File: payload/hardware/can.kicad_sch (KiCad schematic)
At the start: 2 parts, among them U2 MCP2517FD-xJHA, U4 SN65HVD230

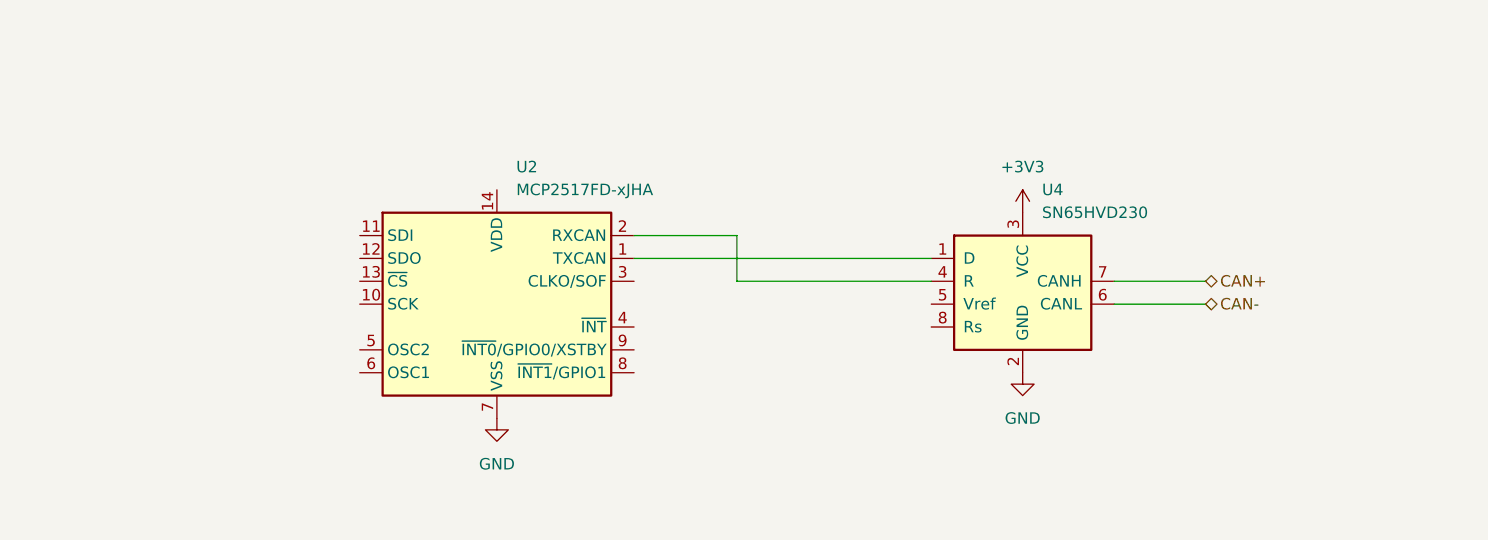
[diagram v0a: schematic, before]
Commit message: add part of a motor driver
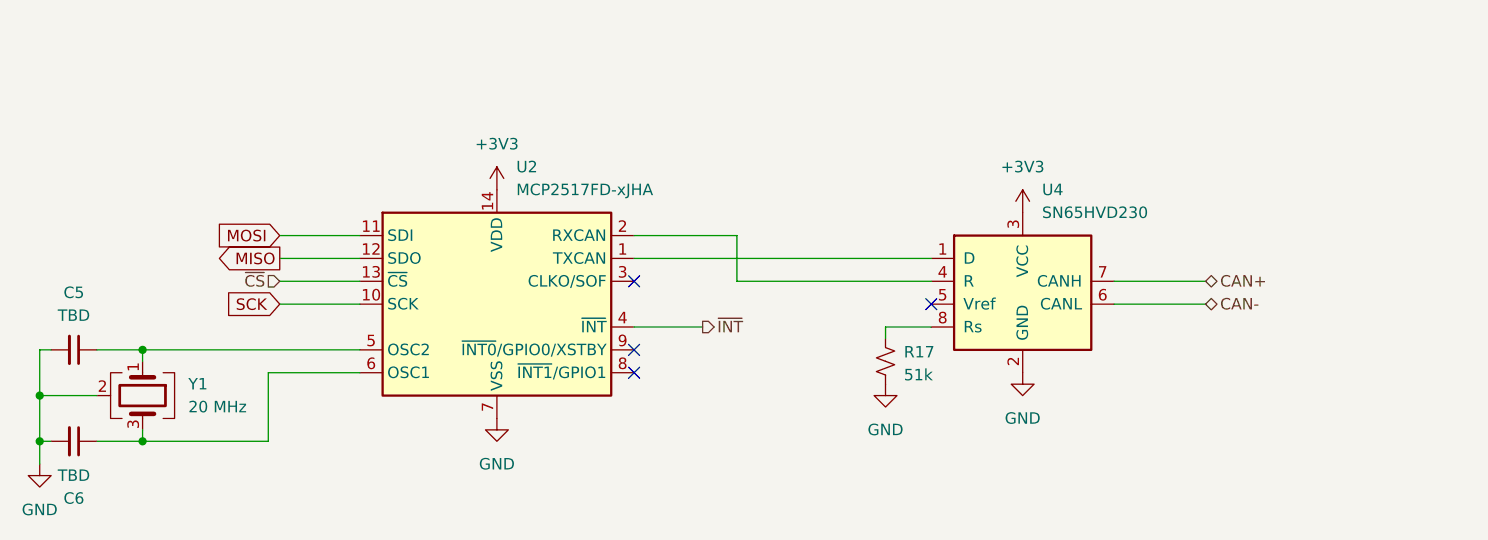
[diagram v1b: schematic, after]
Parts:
- added C5, C6: TBD, Capacitor_SMD:C_0402_1005Metric, symbol Device:C_Small
- added R17: 51k, Resistor_SMD:R_0402_1005Metric, symbol Device:R_Small_US
- added Y1: 20 MHz, Crystal:Crystal_SMD_SeikoEpson_TSX3225-4Pin_3.2x2.5mm, symbol Device:Crystal_GND24
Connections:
- net +3V3: now also U2.14 (VDD)
- net GND: now also C5.2, C6.2, R17.2, Y1.2 (G), Y1.4 (G)
- net SCK: now reaches U2.10 (SCK)
- net MOSI: now reaches U2.11 (SDI)
- net MISO: now reaches U2.12 (SDO)
- net ~{CS}: now reaches U2.13 (~{CS})
- net ~{INT}: now reaches U2.4 (~{INT})
- net at U2.5 (OSC2): now also C5.1, Y1.1
- net at U2.6 (OSC1): now also C6.1, Y1.3
- net at U4.8 (Rs): now also R17.1
- no-connect marks 0 -> 4

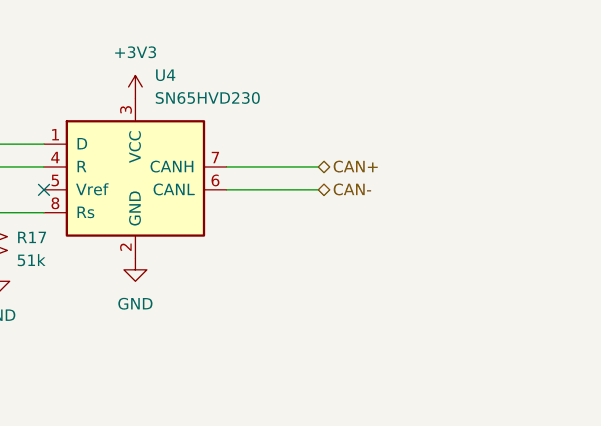
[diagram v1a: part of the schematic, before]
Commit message: finish CANbus schematic and fix USB
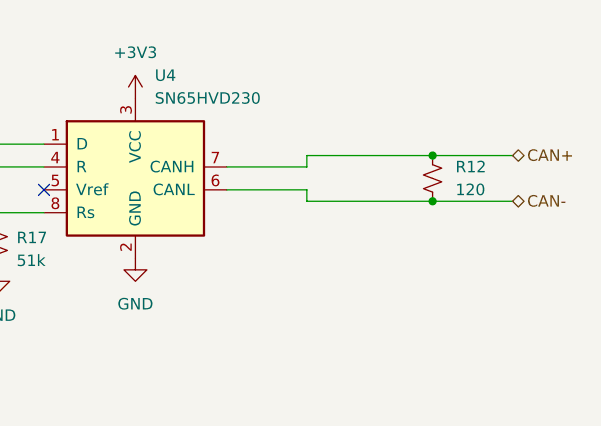
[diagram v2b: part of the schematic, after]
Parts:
- added R12: 120, Resistor_SMD:R_0402_1005Metric, symbol Device:R_Small_US
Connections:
- net CAN+: now also R12.1
- net CAN-: now also R12.2
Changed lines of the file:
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@@
+	)
+	(junction
+		(at 201.93 71.12)
+		(diameter 0)
+		(color 0 0 0 0)
 	)
 	(junction
@@
 		(color 0 0 0 0)
 	)
+	(junction
+		(at 201.93 76.2)
+		(diameter 0)
+		(color 0 0 0 0)
+	)
 	(no_connect
 		(at 125.73 72.39)
@@
 	(wire
 		(pts
+			(xy 187.96 71.12) (xy 187.96 72.39)
+		)
+		(stroke
+			(width 0)
+			(type default)
+		)
+	)
+	(wire
+		(pts
 			(xy 137.16 72.39) (xy 137.16 67.31)
 		)
@@
 	(wire
 		(pts
+			(xy 201.93 71.12) (xy 210.82 71.12)
+		)
+		(stroke
+			(width 0)
+			(type default)
+		)
+	)
+	(wire
+		(pts
 			(xy 86.36 67.31) (xy 95.25 67.31)
 		)
@@
 	(wire
 		(pts
-			(xy 179.07 74.93) (xy 189.23 74.93)
-		)
-		(stroke
-			(width 0)
-			(type default)
-		)
-	)
-	(wire
-		(pts
-			(xy 179.07 72.39) (xy 189.23 72.39)
+			(xy 187.96 76.2) (xy 201.93 76.2)
+		)
+		(stroke
+			(width 0)
+			(type default)
+		)
+	)
+	(wire
+		(pts
+			(xy 187.96 76.2) (xy 187.96 74.93)
+		)
+		(stroke
+			(width 0)
+			(type default)
+		)
+	)
+	(wire
+		(pts
+			(xy 187.96 71.12) (xy 201.93 71.12)
+		)
+		(stroke
+			(width 0)
+			(type default)
+		)
+	)
+	(wire
+		(pts
+			(xy 187.96 72.39) (xy 179.07 72.39)
 		)
 		(stroke
@@
 	(wire
 		(pts
+			(xy 187.96 74.93) (xy 179.07 74.93)
+		)
+		(stroke
+			(width 0)
+			(type default)
+		)
+	)
+	(wire
+		(pts
 			(xy 153.67 77.47) (xy 153.67 78.74)
 		)
@@
 		(pts
 			(xy 85.09 90.17) (xy 85.09 82.55)
+		)
+		(stroke
+			(width 0)
+			(type default)
+		)
+	)
+	(wire
+		(pts
+			(xy 201.93 76.2) (xy 210.82 76.2)
 		)
 		(stroke
@@
 	(hierarchical_label "CAN-"
 		(shape bidirectional)
-		(at 189.23 74.93 0)
+		(at 210.82 76.2 0)
 		(effects
 			(font
@@
 	(hierarchical_label "CAN+"
 		(shape bidirectional)
-		(at 189.23 72.39 0)
+		(at 210.82 71.12 0)
 		(effects
 			(font
@@
 		)
 	)
+	(symbol
+		(lib_id "Device:R_Small_US")
+		(at 201.93 73.66 0)
+		(unit 1)
+		(body_style 1)
+		(exclude_from_sim no)
+		(in_bom yes)
+		(on_board yes)
+		(in_pos_files yes)
+		(dnp no)
+		(fields_autoplaced yes)
+		(property "Reference" "R12"
+			(at 204.47 72.3899 0)
+			(show_name no)
+			(do_not_autoplace no)
+			(effects
+				(font
+					(size 1.27 1.27)
+				)
+				(justify left)
+			)
+		)
+		(property "Value" "120"
+			(at 204.47 74.9299 0)
+			(show_name no)
+			(do_not_autoplace no)
+			(effects
+				(font
+					(size 1.27 1.27)
+				)
+				(justify left)
+			)
+		)
+		(property "Footprint" "Resistor_SMD:R_0402_1005Metric"
+			(at 201.93 73.66 0)
+			(hide yes)
+			(show_name no)
+			(do_not_autoplace no)
+			(effects
+				(font
+					(size 1.27 1.27)
+				)
+			)
+		)
+		(property "Datasheet" ""
+			(at 201.93 73.66 0)
+			(hide yes)
+			(show_name no)
+			(do_not_autoplace no)
+			(effects
+				(font
+					(size 1.27 1.27)
+				)
+			)
+		)
+		(property "Description" "Resistor, small US symbol"
+			(at 201.93 73.66 0)
+			(hide yes)
+			(show_name no)
+			(do_not_autoplace no)
+			(effects
+				(font
+					(size 1.27 1.27)
+				)
+			)
+		)
+		(pin "2"
+		)
+		(pin "1"
+		)
+		(instances
+			(project "payload"
+				(path "/6c55f0ca-d6e4-4a04-9323-ecf7d8843170/2c1b50ef-7864-4a15-8fab-073a91440387/d4b7b76f-24e6-4b2a-a93b-55ace58d0ff9"
+					(reference "R13")
+					(unit 1)
+				)
+				(path "/6c55f0ca-d6e4-4a04-9323-ecf7d8843170/2c1b50ef-7864-4a15-8fab-073a91440387/e8057e65-de86-4674-be4a-6a6d58efe02c"
+					(reference "R12")
+					(unit 1)
+				)
+			)
+		)
+	)

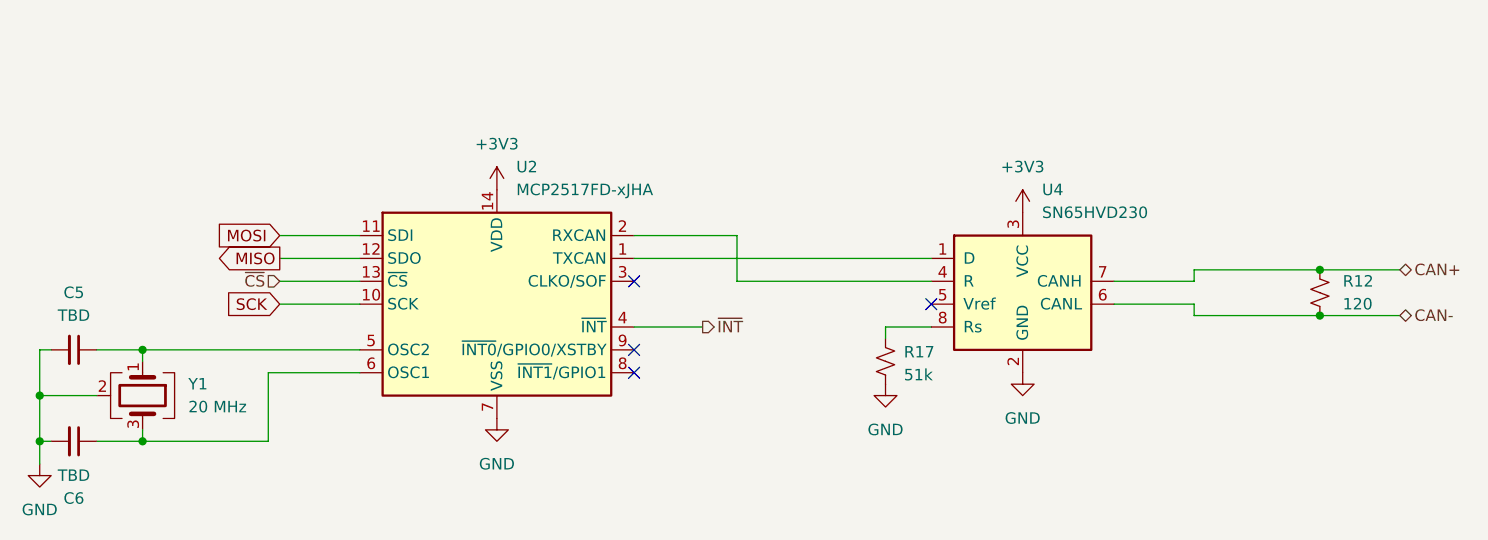
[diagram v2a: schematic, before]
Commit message: add decoupling caps, fix USB skew, add Jax's name
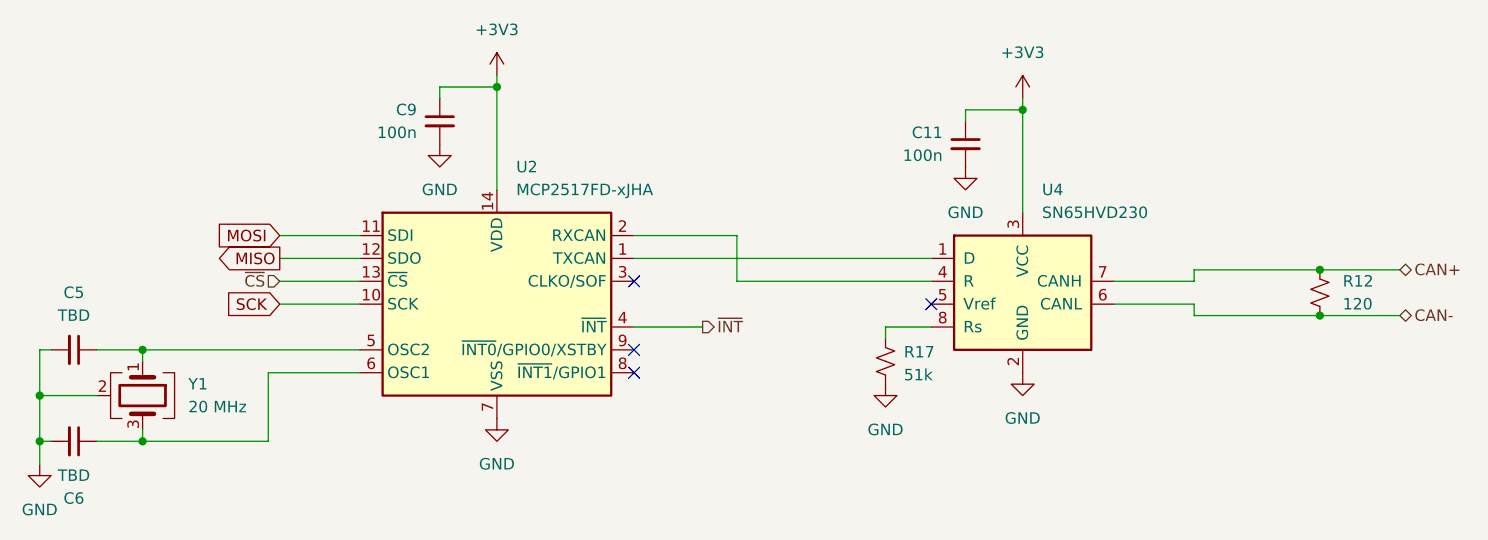
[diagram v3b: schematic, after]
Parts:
- added C11, C9: 100n, Capacitor_SMD:C_0402_1005Metric, symbol Device:C_Small
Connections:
- net +3V3: now also C11.1, C9.1
- net GND: now also C11.2, C9.2

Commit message: ERC fixes, nits, NC
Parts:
- C11, C5, C6, C9: symbol Device:C_Small -> Device:C_Small_US
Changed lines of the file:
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@@
 	)
 	(symbol
-		(lib_id "Device:C_Small")
+		(lib_id "Device:C_Small_US")
 		(at 63.5 80.01 270)
 		(unit 1)
@@
 		(fields_autoplaced yes)
 		(property "Reference" "C5"
-			(at 63.4936 73.66 90)
+			(at 63.373 73.66 90)
 			(show_name no)
 			(do_not_autoplace no)
@@
 		)
 		(property "Value" "TBD"
-			(at 63.4936 76.2 90)
+			(at 63.373 76.2 90)
 			(show_name no)
 			(do_not_autoplace no)
@@
 			)
 		)
-		(property "Description" "Unpolarized capacitor, small symbol"
+		(property "Description" "capacitor, small US symbol"
 			(at 63.5 80.01 0)
 			(hide yes)
@@
 	)
 	(symbol
-		(lib_id "Device:C_Small")
+		(lib_id "Device:C_Small_US")
 		(at 63.5 90.17 270)
 		(mirror x)
@@
 			)
 		)
-		(property "Description" "Unpolarized capacitor, small symbol"
+		(property "Description" "capacitor, small US symbol"
 			(at 63.5 90.17 0)
 			(hide yes)
@@
 	)
 	(symbol
-		(lib_id "Device:C_Small")
+		(lib_id "Device:C_Small_US")
 		(at 104.14 54.61 0)
-		(mirror y)
 		(unit 1)
 		(body_style 1)
@@
 		(in_pos_files yes)
 		(dnp no)
-		(fields_autoplaced yes)
 		(property "Reference" "C9"
-			(at 101.6 53.3462 0)
-			(show_name no)
-			(do_not_autoplace no)
-			(effects
-				(font
-					(size 1.27 1.27)
-				)
-				(justify left)
+			(at 101.6 53.4669 0)
+			(show_name no)
+			(do_not_autoplace no)
+			(effects
+				(font
+					(size 1.27 1.27)
+				)
+				(justify right)
 			)
 		)
 		(property "Value" "100n"
-			(at 101.6 55.8862 0)
-			(show_name no)
-			(do_not_autoplace no)
-			(effects
-				(font
-					(size 1.27 1.27)
-				)
-				(justify left)
+			(at 101.6 56.0069 0)
+			(show_name no)
+			(do_not_autoplace no)
+			(effects
+				(font
+					(size 1.27 1.27)
+				)
+				(justify right)
 			)
 		)
@@
 			)
 		)
-		(property "Description" "Unpolarized capacitor, small symbol"
+		(property "Description" "capacitor, small US symbol"
 			(at 104.14 54.61 0)
 			(hide yes)
@@
 	)
 	(symbol
-		(lib_id "Device:C_Small")
+		(lib_id "Device:C_Small_US")
 		(at 162.56 57.15 0)
-		(mirror y)
 		(unit 1)
 		(body_style 1)
@@
 		(in_pos_files yes)
 		(dnp no)
-		(fields_autoplaced yes)
 		(property "Reference" "C11"
-			(at 160.02 55.8862 0)
-			(show_name no)
-			(do_not_autoplace no)
-			(effects
-				(font
-					(size 1.27 1.27)
-				)
-				(justify left)
+			(at 160.02 56.0069 0)
+			(show_name no)
+			(do_not_autoplace no)
+			(effects
+				(font
+					(size 1.27 1.27)
+				)
+				(justify right)
 			)
 		)
 		(property "Value" "100n"
-			(at 160.02 58.4262 0)
-			(show_name no)
-			(do_not_autoplace no)
-			(effects
-				(font
-					(size 1.27 1.27)
-				)
-				(justify left)
+			(at 160.02 58.5469 0)
+			(show_name no)
+			(do_not_autoplace no)
+			(effects
+				(font
+					(size 1.27 1.27)
+				)
+				(justify right)
 			)
 		)
@@
 			)
 		)
-		(property "Description" "Unpolarized capacitor, small symbol"
+		(property "Description" "capacitor, small US symbol"
 			(at 162.56 57.15 0)
 			(hide yes)

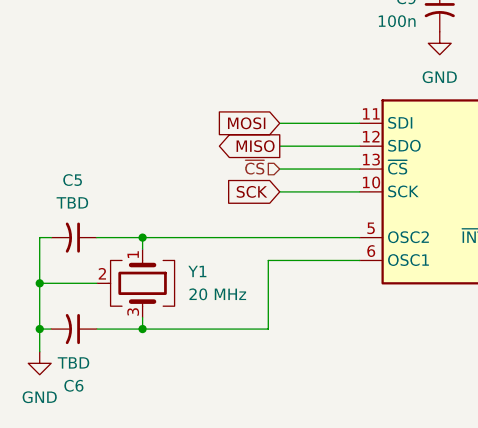
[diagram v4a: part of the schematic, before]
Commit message: add digikey part numbers
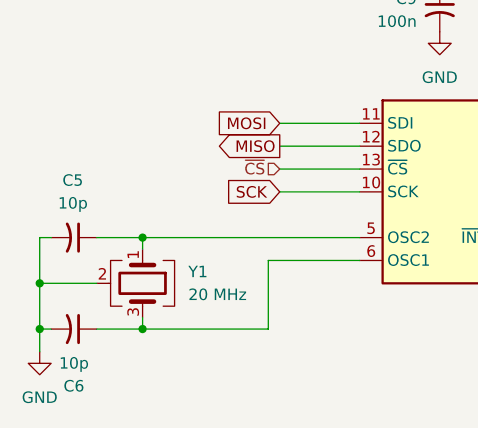
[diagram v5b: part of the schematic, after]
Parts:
- C11, C9: Digikey (none) -> 1276-1001-1-ND
- C5, C6: value TBD -> 10p; Digikey (none) -> 490-10668-1-ND
- R12: Digikey (none) -> YAG3440CT-ND
- R17: Digikey (none) -> 13-RC0402FR-1351KLCT-ND
- U2: Digikey (none) -> MCP2517FDT-H/JHACT-ND
- U4: Digikey (none) -> 296-11654-1-ND
- Y1: Digikey (none) -> SER3629CT-ND
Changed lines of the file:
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@@
+			)
+		)
+		(property "Digikey" "YAG3440CT-ND"
+			(at 201.93 73.66 0)
+			(hide yes)
+			(show_name no)
+			(do_not_autoplace no)
+			(effects
+				(font
+					(size 1.27 1.27)
+				)
 			)
 		)
@@
 			)
 		)
+		(property "Digikey" "MCP2517FDT-H/JHACT-ND"
+			(at 110.49 74.93 0)
+			(hide yes)
+			(show_name no)
+			(do_not_autoplace no)
+			(effects
+				(font
+					(size 1.27 1.27)
+				)
+			)
+		)
 		(pin "15"
 		)
@@
 			)
 		)
-		(property "Value" "TBD"
+		(property "Value" "10p"
 			(at 63.373 76.2 90)
 			(show_name no)
@@
 		)
 		(property "SnapEDA_Link" ""
+			(at 63.5 80.01 90)
+			(hide yes)
+			(show_name no)
+			(do_not_autoplace no)
+			(effects
+				(font
+					(size 1.27 1.27)
+				)
+			)
+		)
+		(property "Digikey" "490-10668-1-ND"
 			(at 63.5 80.01 90)
 			(hide yes)
@@
 			)
 		)
+		(property "Digikey" "13-RC0402FR-1351KLCT-ND"
+			(at 153.67 81.28 0)
+			(hide yes)
+			(show_name no)
+			(do_not_autoplace no)
+			(effects
+				(font
+					(size 1.27 1.27)
+				)
+			)
+		)
 		(pin "2"
 		)
@@
 			)
 		)
-		(property "Value" "TBD"
+		(property "Value" "10p"
 			(at 63.4936 93.98 90)
 			(show_name no)
@@
 		)
 		(property "SnapEDA_Link" ""
+			(at 63.5 90.17 90)
+			(hide yes)
+			(show_name no)
+			(do_not_autoplace no)
+			(effects
+				(font
+					(size 1.27 1.27)
+				)
+			)
+		)
+		(property "Digikey" "490-10668-1-ND"
 			(at 63.5 90.17 90)
 			(hide yes)
@@
 		)
 		(property "Description" "capacitor, small US symbol"
+			(at 104.14 54.61 0)
+			(hide yes)
+			(show_name no)
+			(do_not_autoplace no)
+			(effects
+				(font
+					(size 1.27 1.27)
+				)
+			)
+		)
+		(property "Digikey" "1276-1001-1-ND"
 			(at 104.14 54.61 0)
 			(hide yes)
@@
 			)
 		)
+		(property "Digikey" "SER3629CT-ND"
+			(at 71.12 85.09 90)
+			(hide yes)
+			(show_name no)
+			(do_not_autoplace no)
+			(effects
+				(font
+					(size 1.27 1.27)
+				)
+			)
+		)
 		(pin "1"
 		)
@@
 			)
 		)
+		(property "Digikey" "1276-1001-1-ND"
+			(at 162.56 57.15 0)
+			(hide yes)
+			(show_name no)
+			(do_not_autoplace no)
+			(effects
+				(font
+					(size 1.27 1.27)
+				)
+			)
+		)
 		(pin "2"
 		)
@@
 			(at 168.91 72.39 0)
 			(hide yes)
+			(show_name no)
+			(do_not_autoplace no)
+			(effects
+				(font
+					(size 1.27 1.27)
+				)
+			)
+		)
+		(property "Digikey" "296-11654-1-ND"
+			(at 168.91 72.39 0)
+			(hide yes)
